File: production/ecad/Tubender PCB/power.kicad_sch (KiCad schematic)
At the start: 0 parts

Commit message: Added 3V3 buck circuitry to main branch, added 3V3 label
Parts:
- added CBOOT1: 0.1u, symbol Device:C_Small
- added CIN1: 4.7u, symbol Device:C_Small
- added C_HF1: 220n, symbol Device:C_Small
- added C_OUT1: 22u, symbol Device:C_Small
- added C_VCC1: 1u, symbol Device:C
- added L1: 8.5u, symbol Device:L
- added R1: 43.5k, symbol Device:R_Small_US
- added R2: 100k, symbol Device:R_Small_US
- added R3: 100k, symbol Device:R_US
- added U1: LMR36520FADDAR, LMR36520FADDAR:IC_LMR36520FADDAR, symbol LMR36520FADDAR:LMR36520FADDAR
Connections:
- new net: C_VCC1.1, U1.6 (VCC)
- new net: R3.2, U1.4 (PG)
- new net: R1.2, R2.1, U1.5 (FB)
- new net: CBOOT1.2, U1.7 (BOOT)
- new net: CBOOT1.1, L1.2, U1.8 (SW)
- new net +48V: CIN1.1, C_HF1.1, U1.2 (VIN), U1.3 (EN)
- new net 3V3: C_OUT1.2, L1.1, R2.2
- new net GND: CIN1.2, C_HF1.2, C_OUT1.1, C_VCC1.2, R1.1, R3.1, U1.1 (PGND), U1.10 (EP), U1.11 (EP), U1.12 (EP), U1.13 (EP), U1.14 (EP), U1.15 (EP), U1.9 (EP)
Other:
- note added: "3.3V Buck Circuit"

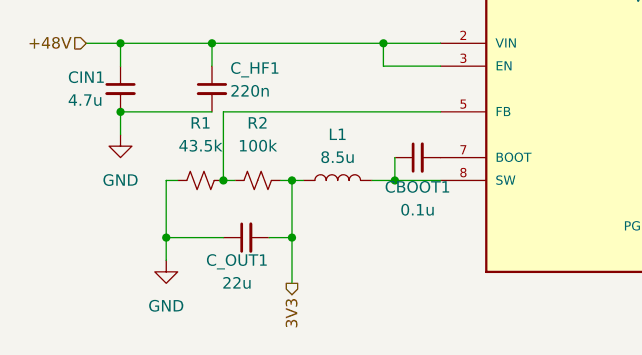
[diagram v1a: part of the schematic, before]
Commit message: 3V3 output cap value change based on phase margin
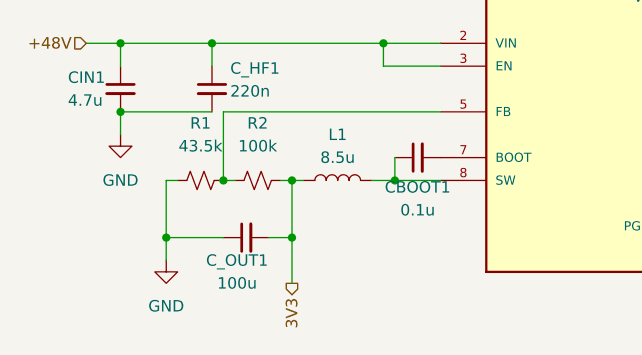
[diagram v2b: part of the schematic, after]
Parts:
- C_OUT1: value 22u -> 100u
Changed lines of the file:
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@@
 			)
 		)
-		(property "Value" "22u"
+		(property "Value" "100u"
 			(at 48.514 67.31 90)
 			(effects

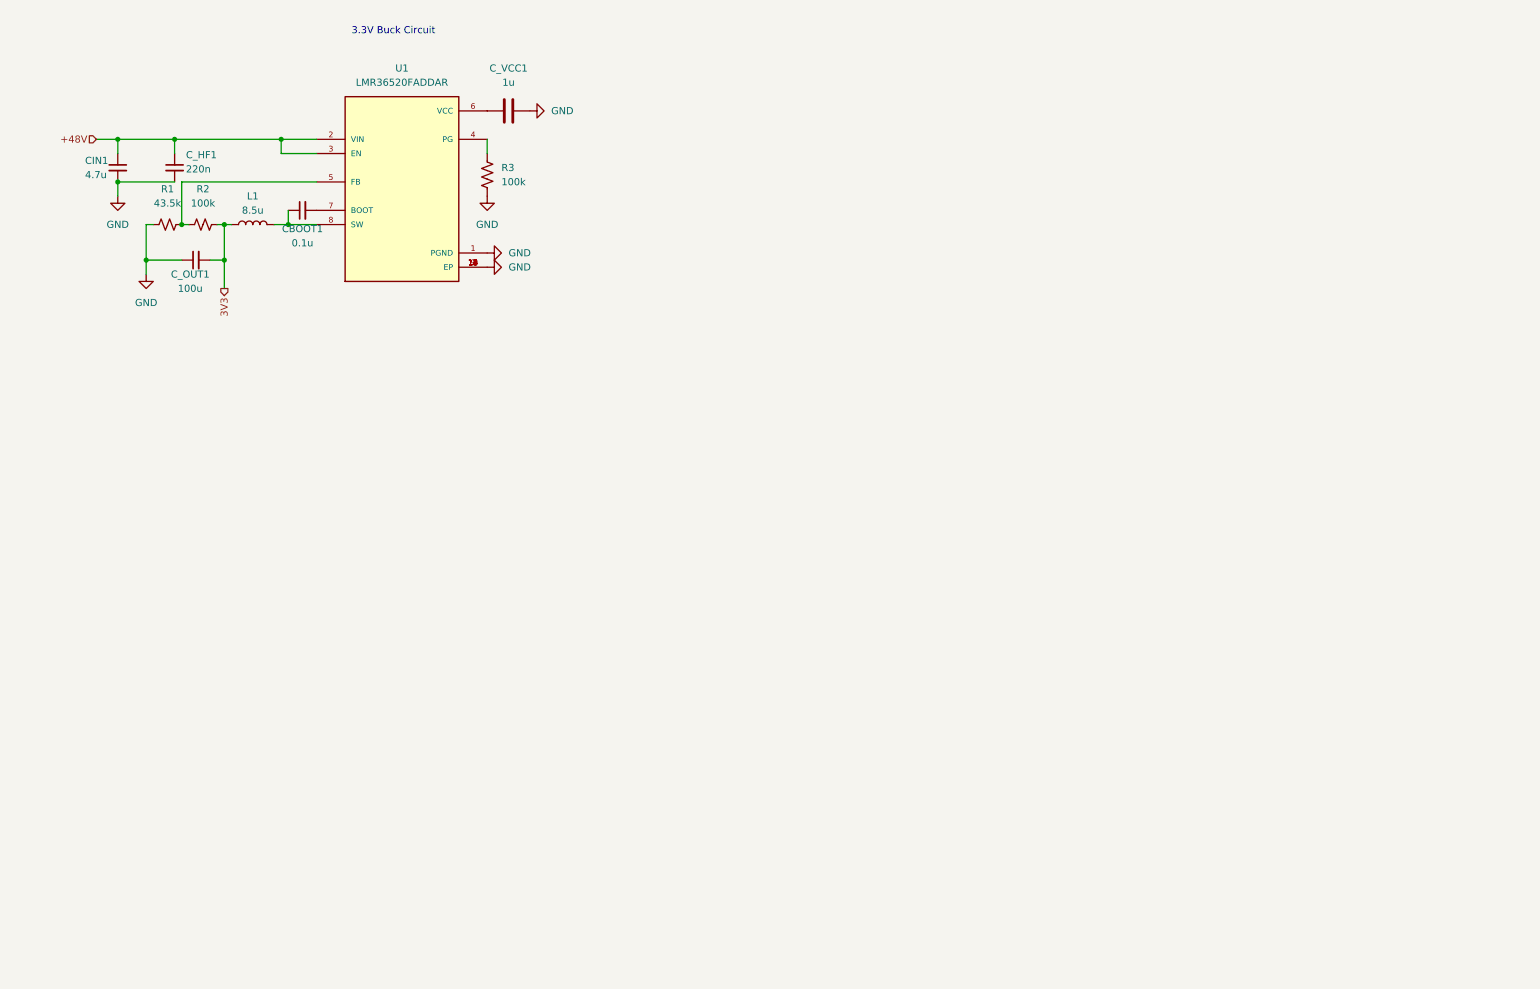
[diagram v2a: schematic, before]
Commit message: Added IC and some connections for 12V buck. Added 12V output connection
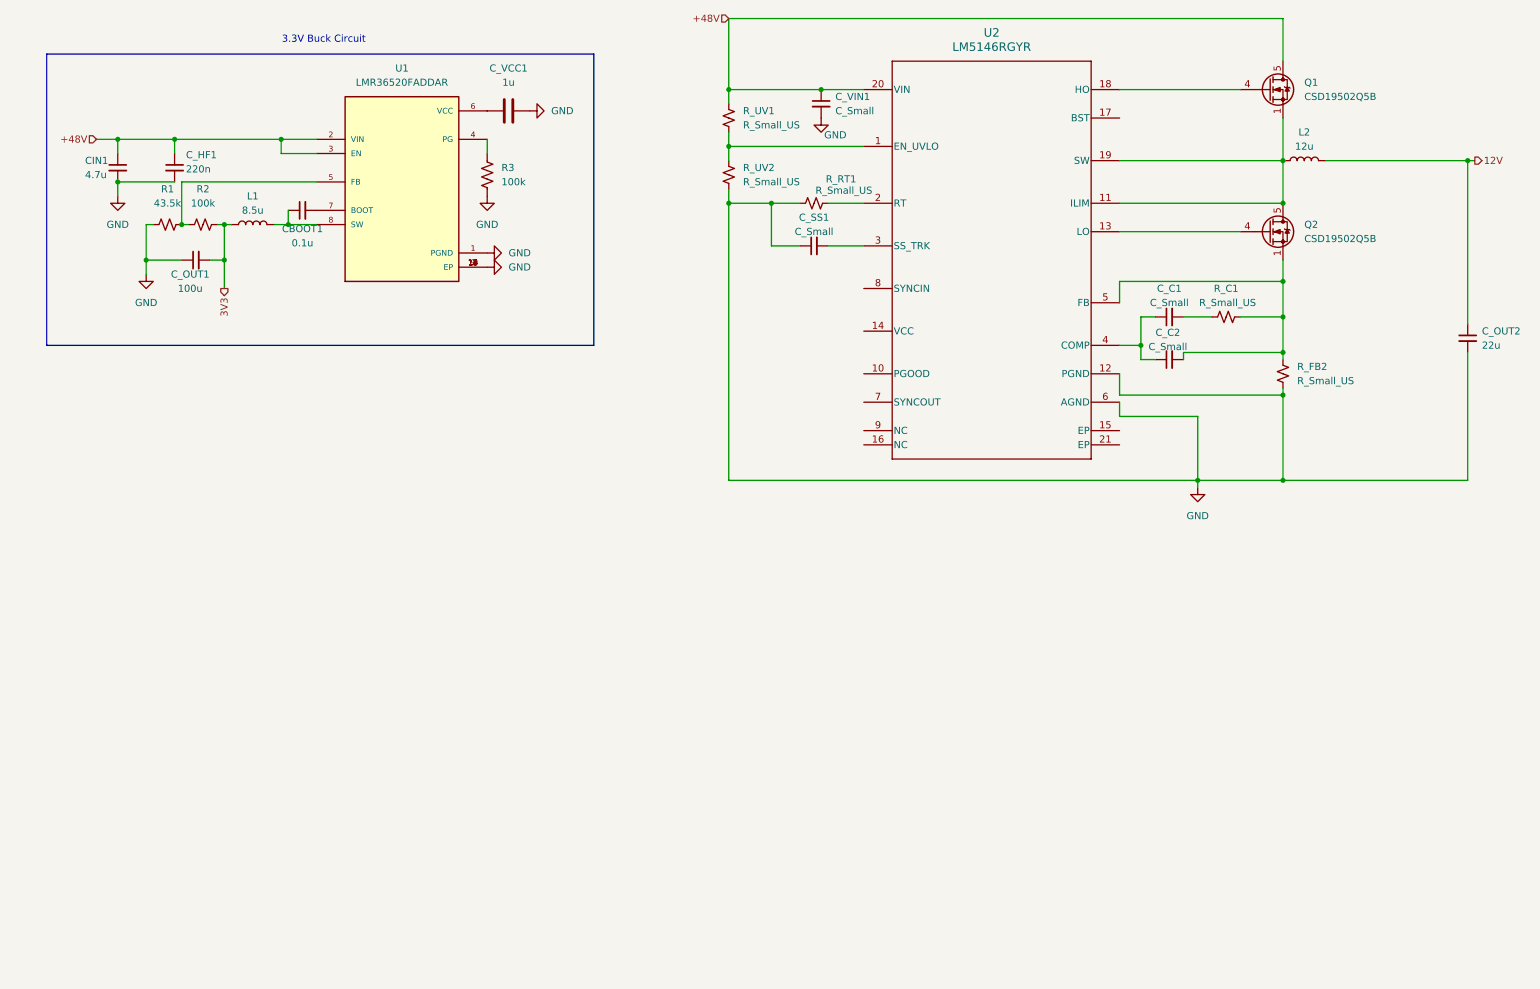
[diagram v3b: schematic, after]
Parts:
- added C_C1, C_C2, C_SS1, C_VIN1: C_Small, symbol Device:C_Small
- added C_OUT2: 22u, symbol Device:C_Small
- added L2: 12u, symbol Device:L
- added Q1, Q2: CSD19502Q5B, Package_TO_SOT_SMD:TDSON-8-1, symbol Transistor_FET:CSD19502Q5B
- added R_C1, R_FB2, R_RT1, R_UV1, R_UV2: R_Small_US, symbol Device:R_Small_US
- added U2: LM5146RGYR, RGY0020B-MFG, symbol RGY0020B-MFG:LM5146RGYR
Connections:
- net +48V: now also C_VIN1.1, Q1.5 (D), R_UV1.1, U2.20 (VIN)
- net GND: now also C_OUT2.2, C_SS1.1, C_VIN1.2, R_FB2.2, R_RT1.1, R_UV2.2, U2.12 (PGND), U2.6 (AGND)
- new net: L2.1, Q1.1 (S), Q1.2 (S), Q1.3 (S), Q2.5 (D), U2.11 (ILIM), U2.19 (SW)
- new net: Q1.4 (G), U2.18 (HO)
- new net: R_UV1.2, R_UV2.1, U2.1 (EN_UVLO)
- new net: Q2.4 (G), U2.13 (LO)
- new net: R_RT1.2, U2.2 (RT)
- new net: C_SS1.2, U2.3 (SS_TRK)
- new net: C_C1.1, C_C2.1, U2.4 (COMP)
- new net: C_C2.2, Q2.1 (S), Q2.2 (S), Q2.3 (S), R_C1.2, R_FB2.1, U2.5 (FB)
- new net: C_C1.2, R_C1.1
- new net 12V: C_OUT2.1, L2.2

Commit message: All passives valued for 12V buck
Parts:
- removed Q2: CSD19502Q5B, Package_TO_SOT_SMD:TDSON-8-1, symbol Transistor_FET:CSD19502Q5B
- added C_BST2: 100n, symbol Device:C_Small
- added C_C3: 1n, symbol Device:C_Small
- added C_ILIM: 3p, symbol Device:C_Small
- added C_IN2: 4.7u, symbol Device:C_Small
- added C_VCC2: 2.2u, symbol Device:C_Small
- added Q2: CSD19534Q5A, Package_TO_SOT_SMD:TDSON-8-1, symbol Transistor_FET:CSD19534Q5A
- added R_C2: 40, symbol Device:R_Small_US
- added R_FB1: 18k, symbol Device:R_Small_US
- added R_ILIM: 1k, symbol Device:R_Small_US
- added R_PG1, R_VCC: 20k, symbol Device:R_Small_US
- C_C1: value C_Small -> 6.8n
- C_C2: value C_Small -> 312p
- C_SS1: value C_Small -> 12.5n
- C_VIN1: value C_Small -> 100n
- R_C1: value R_Small_US -> 4k
- R_FB2: value R_Small_US -> 1290
- R_RT1: value R_Small_US -> 39.2k
- R_UV1: value R_Small_US -> 237k
- R_UV2: value R_Small_US -> 7.6k
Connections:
- net +48V: now also C_IN2.1; no longer C_VIN1.1, R_UV1.1, U2.20 (VIN)
- net 12V: now also R_C2.1, R_FB1.1
- net GND: now also C_ILIM.1, C_IN2.2, C_VCC2.2
- net at L2.1, Q1.1 (S), Q1.2 (S)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: now also C_BST2.2, Q2.5 (D), R_ILIM.2; no longer U2.11 (ILIM)
- net at U2.10 (PGOOD): now also R_PG1.2
- net at U2.13 (LO): now also Q2.4 (G)
- net at U2.14 (VCC): now also C_VCC2.1, R_PG1.1, R_VCC.2
- net at U2.17 (BST): now also C_BST2.1
- net at C_C2.2, R_C1.2, R_FB2.1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: now also C_C3.2, Q2.1 (S), Q2.2 (S), Q2.3 (S), R_FB1.2
- net at U2.8 (SYNCIN): now also R_VCC.1
- new net: C_ILIM.2, R_ILIM.1, U2.11 (ILIM)
- new net: C_VIN1.1, R_UV1.1, U2.20 (VIN)
- new net: C_C3.1, R_C2.2
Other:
- moved on the sheet: C_C1, C_C2, C_SS1, C_VIN1, L2, Q1, R_C1, R_FB2, R_RT1, R_UV1, R_UV2, U2

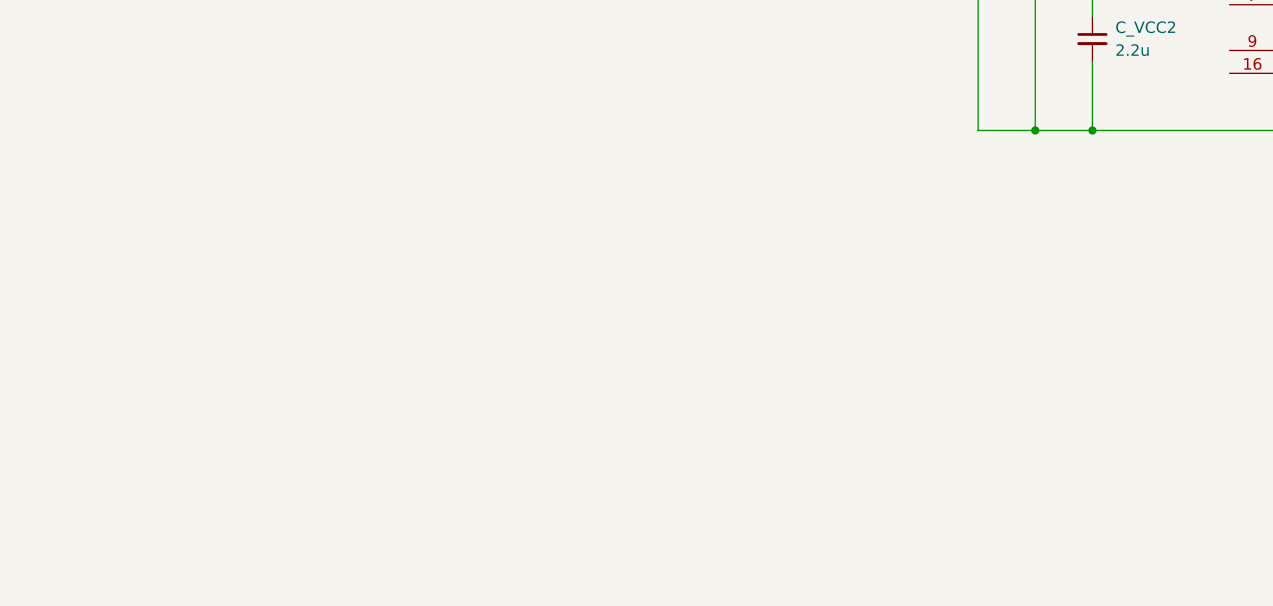
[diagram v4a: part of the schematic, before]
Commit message: Add 5V 20mA buck, symbol, footprint, and datasheet
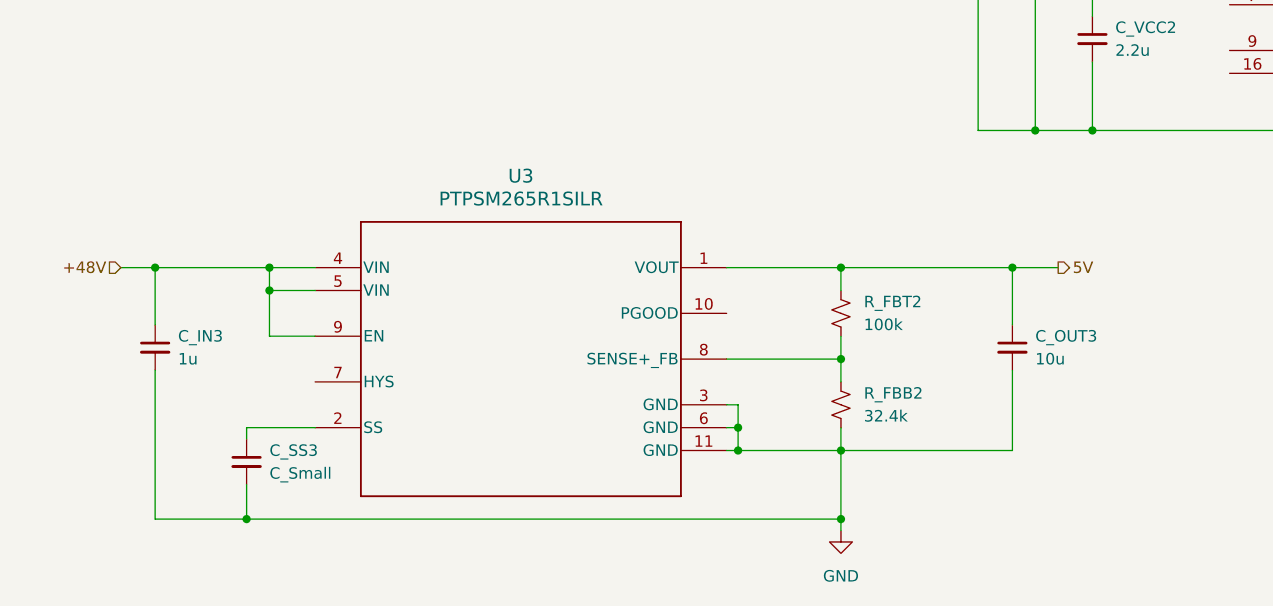
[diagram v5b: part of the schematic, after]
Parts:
- added C_IN3: 1u, symbol Device:C_Small
- added C_OUT3: 10u, symbol Device:C_Small
- added C_SS3: C_Small, symbol Device:C_Small
- added R_FBB2: 32.4k, symbol Device:R_Small_US
- added R_FBT2: 100k, symbol Device:R_Small_US
- added U3: PTPSM265R1SILR, SIL0010C, symbol TPSM265R1V5:PTPSM265R1SILR
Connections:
- net +48V: now also C_IN3.1, U3.4 (VIN), U3.5 (VIN), U3.9 (EN)
- net GND: now also C_IN3.2, C_OUT3.2, C_SS3.2, R_FBB2.2, U3.11 (GND), U3.3 (GND), U3.6 (GND)
- new net: C_SS3.1, U3.2 (SS)
- new net: R_FBB2.1, R_FBT2.2, U3.8 (SENSE+_FB)
- new net 5V: C_OUT3.1, R_FBT2.1, U3.1 (VOUT)

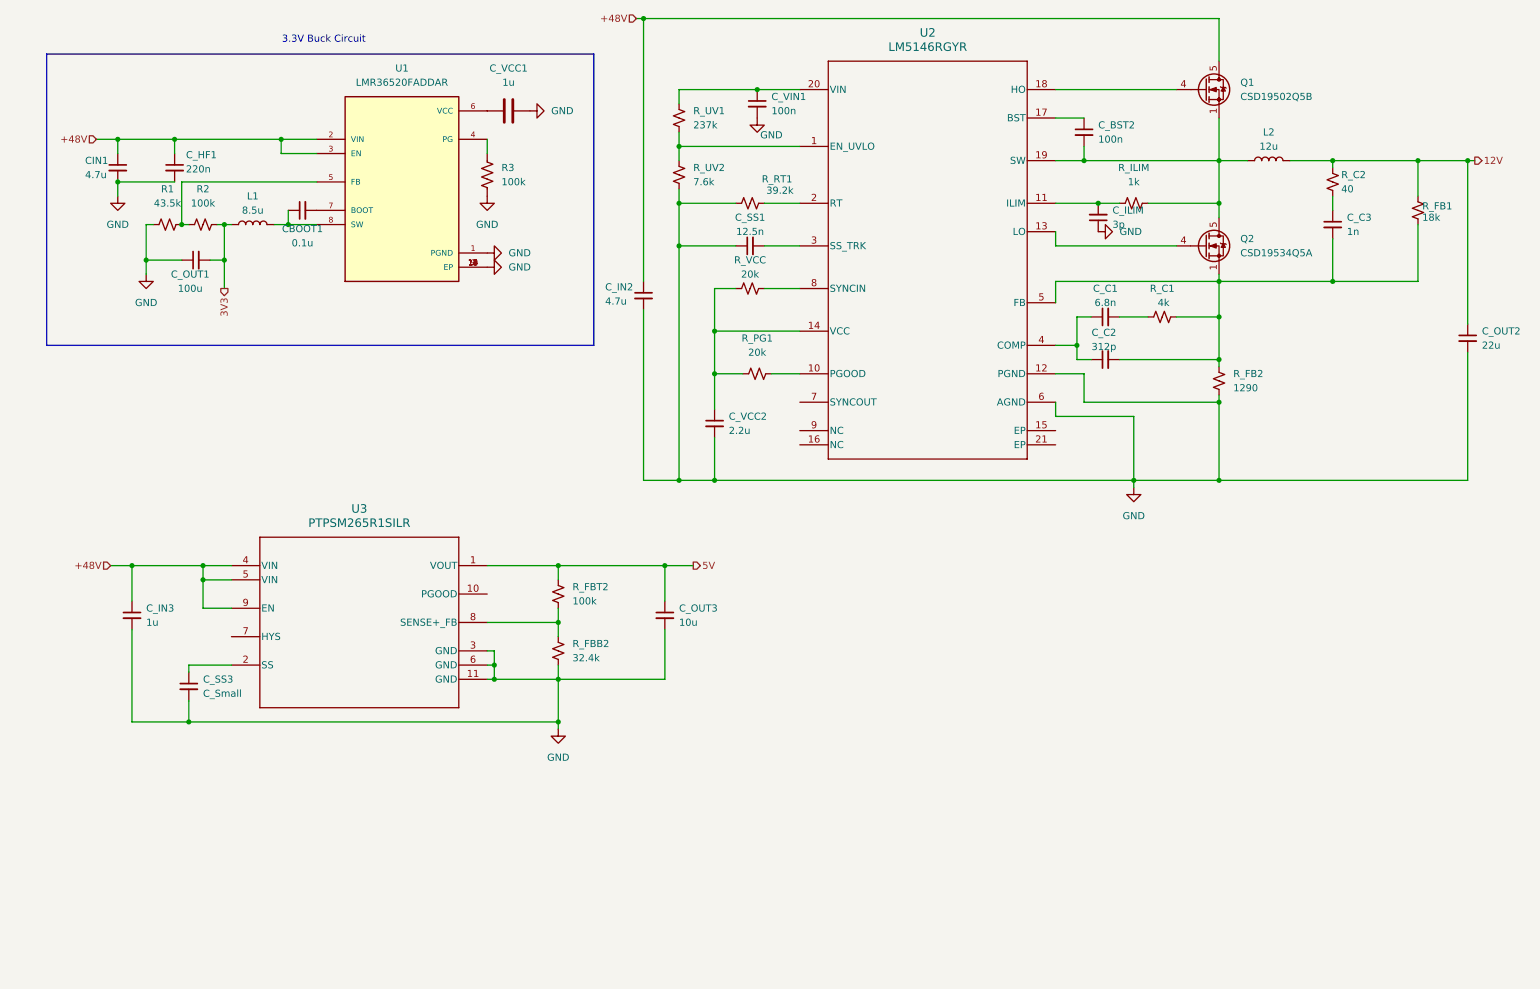
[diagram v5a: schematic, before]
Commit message: add box to identify 12V and 5V buck
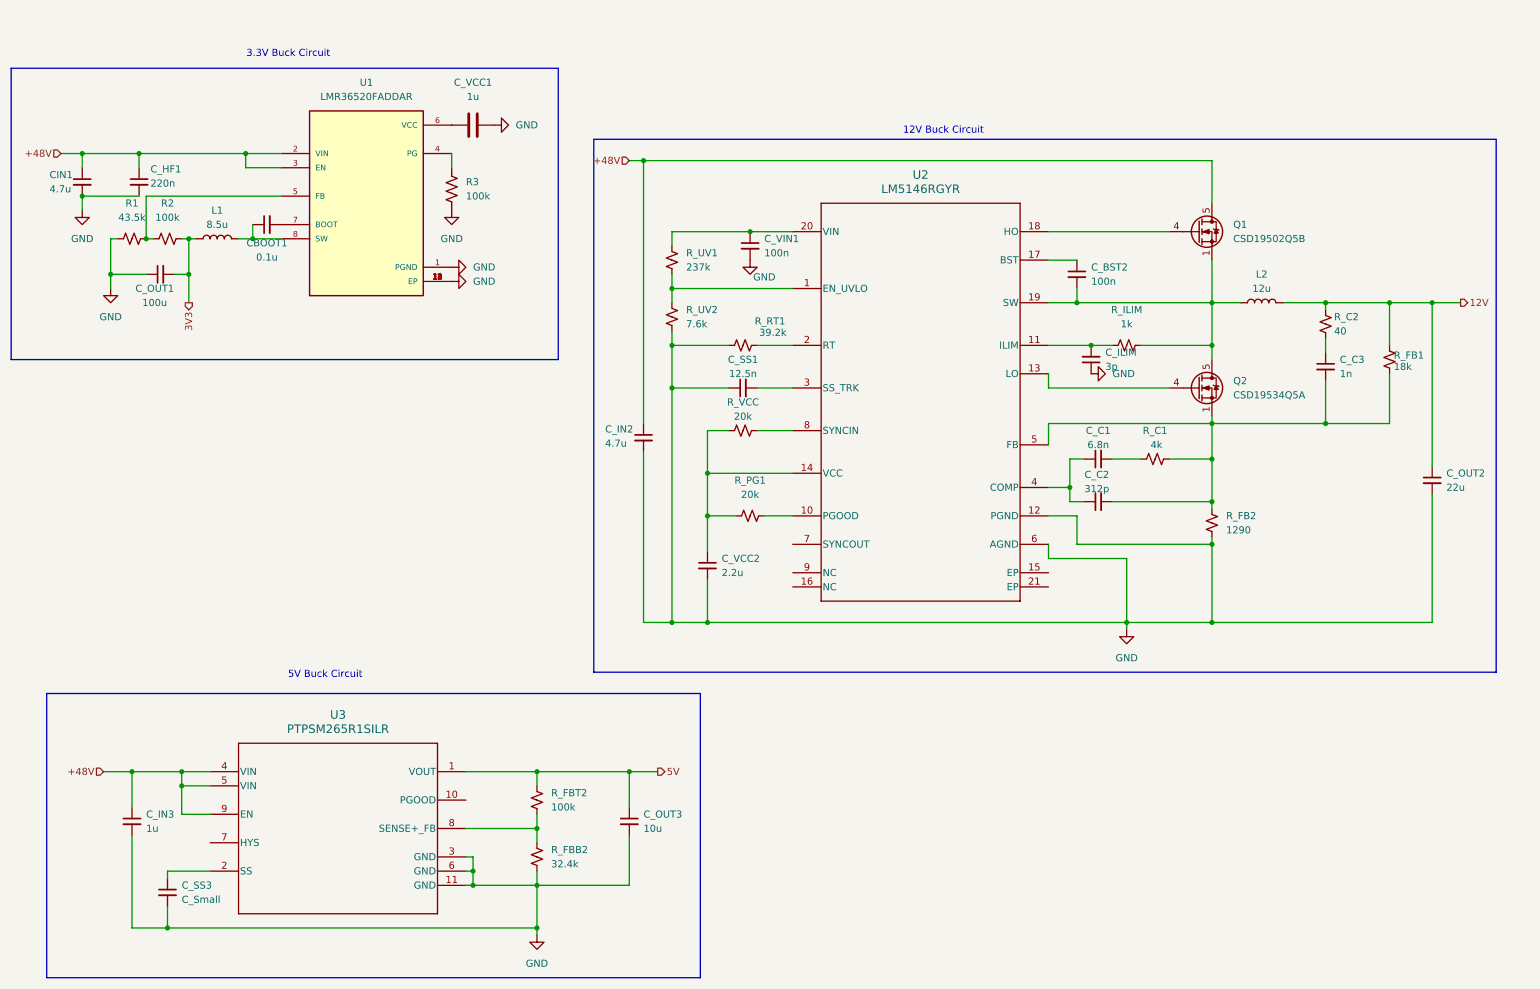
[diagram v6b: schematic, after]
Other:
- note added: "12V Buck Circuit"
- note added: "5V Buck Circuit"
- moved on the sheet: CBOOT1, CIN1, C_BST2, C_C1, C_C2, C_C3, C_HF1, C_ILIM, C_IN2, C_IN3, C_OUT1, C_OUT2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

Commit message: names and stuff
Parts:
- removed R_FBB2: 32.4k, symbol Device:R_Small_US
- removed R_FBT2: 100k, symbol Device:R_Small_US
- removed U3: PTPSM265R1SILR, SIL0010C, symbol TPSM265R1V5:PTPSM265R1SILR
- added U3: TPSM265R1V5SILR, TPSM265R1V5SILR:CONV_TPSM265R1V5SILR, symbol TPSM265R1V5SILR:TPSM265R1V5SILR
- C_SS3: value C_Small -> 8.2n
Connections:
- net +48V: now also U3.4_5 (VIN), U3.9 (EN)
- net 5V: now also U3.1 (VOUT), U3.8 (SENSE+/FB)
- net GND: now also U3.3_6_11 (GND)
- net at C_SS3.1: now also U3.2 (SS)
- no-connect marks 0 -> 3
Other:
- moved on the sheet: C_IN3, C_OUT3, C_SS3
